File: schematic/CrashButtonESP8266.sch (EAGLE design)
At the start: 15 parts, among them U1 ESP12E_DEVKIT

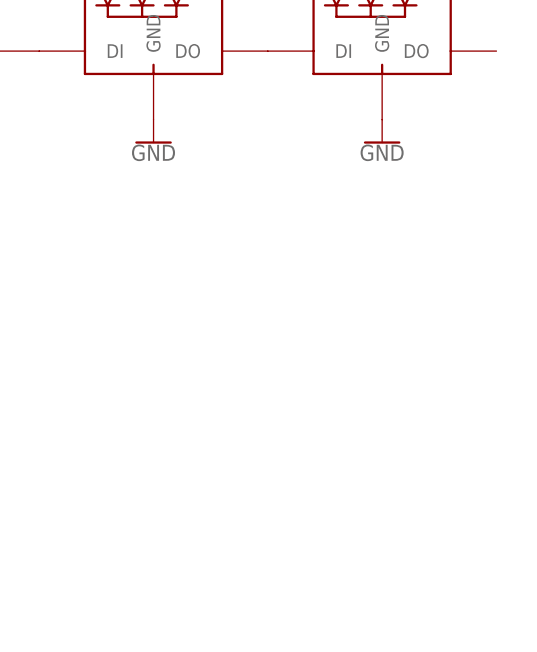
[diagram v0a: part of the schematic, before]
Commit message: circular layout
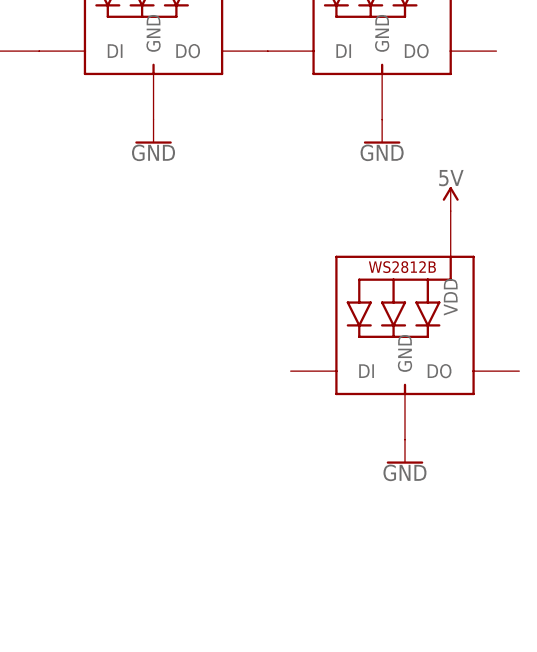
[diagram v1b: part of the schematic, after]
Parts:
- added LED12: WS2812B5050, adafruit:WS2812B5050
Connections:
- net 5V: now also LED12.VDD
- net GND: now also LED12.GND
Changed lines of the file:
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@@
 <part name="R1" library="SparkFun-Resistors" deviceset="470OHM" device="-0603-1/10W-1%" value="470"/>
 <part name="S2" library="SparkFun-Switches" deviceset="MOMENTARY-SWITCH-SPST" device="-PTH-12MM"/>
+<part name="LED12" library="adafruit" deviceset="WS2812B" device="5050"/>
+<part name="GND14" library="SparkFun-PowerSymbols" deviceset="GND" device=""/>
+<part name="SUPPLY13" library="SparkFun-PowerSymbols" deviceset="5V" device=""/>
 </parts>
 <sheets>
@@
 <instance part="R1" gate="G$1" x="81.28" y="15.24"/>
 <instance part="S2" gate="G$1" x="38.1" y="22.86" rot="MR0"/>
+<instance part="LED12" gate="G$1" x="284.48" y="45.72"/>
+<instance part="GND14" gate="1" x="284.48" y="33.02"/>
+<instance part="SUPPLY13" gate="G$1" x="289.56" y="60.96"/>
 </instances>
 <busses>
@@
 <wire x1="129.54" y1="45.72" x2="142.24" y2="45.72" width="0.1524" layer="91"/>
 </segment>
+<segment>
+<pinref part="LED12" gate="G$1" pin="GND"/>
+<pinref part="GND14" gate="1" pin="GND"/>
+</segment>
 </net>
 <net name="5V" class="0">
@@
 <wire x1="134.62" y1="48.26" x2="134.62" y2="50.8" width="0.1524" layer="91"/>
 </segment>
-</net>
+<segment>
+<pinref part="LED12" gate="G$1" pin="VDD"/>
+<pinref part="SUPPLY13" gate="G$1" pin="5V"/>
+</segment>
+</net>

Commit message: moved buttoncheck to ledticker, moved ledpin to D4 in case I want to use NeoPixelBus
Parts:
- added C1, C10, C11, C12, C14, C2, C3, C4, C5, C6, C7, C8, C9: 0.1uF, SparkFun-Capacitors:0.1UF-0603-25V-(+80/-20%)
- added C13: 330uF, SparkFun-Capacitors:100UF-POLAR-RADIAL-2.5MM-25V-20%
- added D1: 200mA/100V/1V, SparkFun-DiscreteSemi:DIODE-1N4148
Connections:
- new net N$12: LED7.DO, LED8.DI
- new net N$13: LED11.DO, LED12.DI
- new net N$14: C13.+, C14.1, D1.A, U1.VIN
- new net VCC: C1.1, C2.1, C3.1, C4.1, C5.1, C6.1, C7.1, C8.1, C9.1, D1.C, LED1.VDD, LED2.VDD, LED3.VDD, LED4.VDD, LED5.VDD, LED6.VDD, LED7.VDD, LED8.VDD, LED9.VDD
- net 5V: now also C10.1, C11.1, C12.1; no longer LED1.VDD, LED2.VDD, LED3.VDD, LED4.VDD, LED5.VDD, LED6.VDD, LED7.VDD, LED8.VDD, LED9.VDD, U1.VIN
- net GND: now also C1.2, C10.2, C11.2, C12.2, C13.-, C14.2, C2.2, C3.2, C4.2, C5.2, C6.2, C7.2, C8.2, C9.2
- net LEDDIN: now also R1.1
- net N$10: now also U1.D2

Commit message: version with enough polygon isolate to be solderable when othermilled
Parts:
- C13: value 330uF -> 1mF; device SparkFun-Capacitors:100UF-POLAR-RADIAL-2.5MM-25V-20% -> SparkFun-Capacitors:1000UF-RADIAL-5MM-25V-20%
- D1: value 200mA/100V/1V -> 250mA/100V; device SparkFun-DiscreteSemi:DIODE-1N4148 -> SparkFun-DiscreteSemi:DIODE-BAS16J
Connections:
- removed net 5V: C10.1, C11.1, C12.1, LED10.VDD, LED11.VDD, LED12.VDD
- removed net N$14: C13.+, C14.1, D1.A, U1.VIN
- new net VIN: C10.1, C11.1, C12.1, C13.+, C14.1, C2.1, C3.1, C4.1, C5.1, C6.1, C7.1, C8.1, C9.1, D1.A, LED10.VDD, LED11.VDD, LED12.VDD, LED2.VDD, LED3.VDD, LED4.VDD, LED5.VDD, LED6.VDD, LED7.VDD, LED8.VDD, LED9.VDD, U1.VIN
- net N$11: now also U1.D4; no longer U1.D1
- net VCC: no longer C2.1, C3.1, C4.1, C5.1, C6.1, C7.1, C8.1, C9.1, LED2.VDD, LED3.VDD, LED4.VDD, LED5.VDD, LED6.VDD, LED7.VDD, LED8.VDD, LED9.VDD
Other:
- moved on the sheet: C13, C14, D1, R1, S1, S2, U1
